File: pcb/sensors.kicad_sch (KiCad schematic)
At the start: 10 parts, among them U2 HDC1080, U3 LTR-303ALS-01, U8 SGP40-D-R4

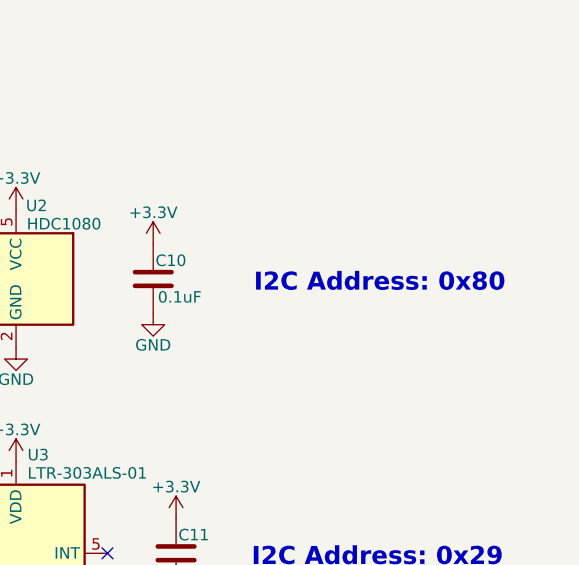
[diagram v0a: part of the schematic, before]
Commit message: Updated LTR address to 0x40 rather than 0x80
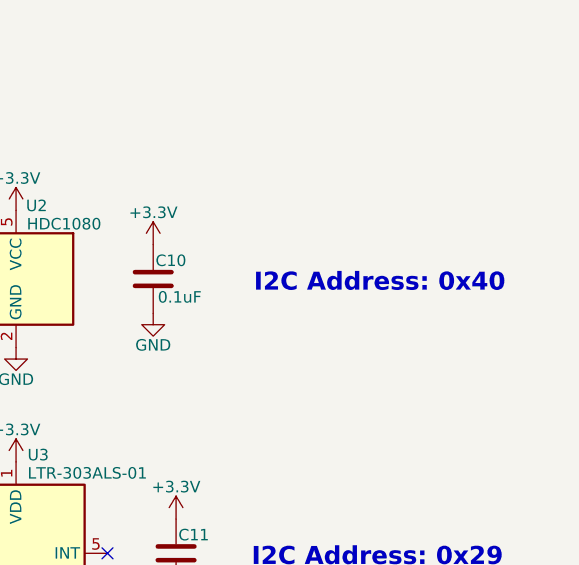
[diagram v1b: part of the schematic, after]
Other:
- note added: "I2C Address: 0x40"
- note removed: "I2C Address: 0x80"
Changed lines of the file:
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@@
 		(comment 1 "<<hash>>")
 	)
-	(text "I2C Address: 0x80"
+	(text "I2C Address: 0x40"
 		(exclude_from_sim no)
 		(at 121.666 50.038 0)
